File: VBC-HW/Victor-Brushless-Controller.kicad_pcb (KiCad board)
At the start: 2 copper layers, 44 x 44 mm, 85 parts, among them J1 i2c QWIIC, P1 V+, P2 GND, Q1 TPH4R008NH, Q2 TPH4R008NH, Q3 TPH4R008NH, Q4 TPH4R008NH, Q5 TPH4R008NH, Q6 TPH4R008NH, SW1 BOOT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

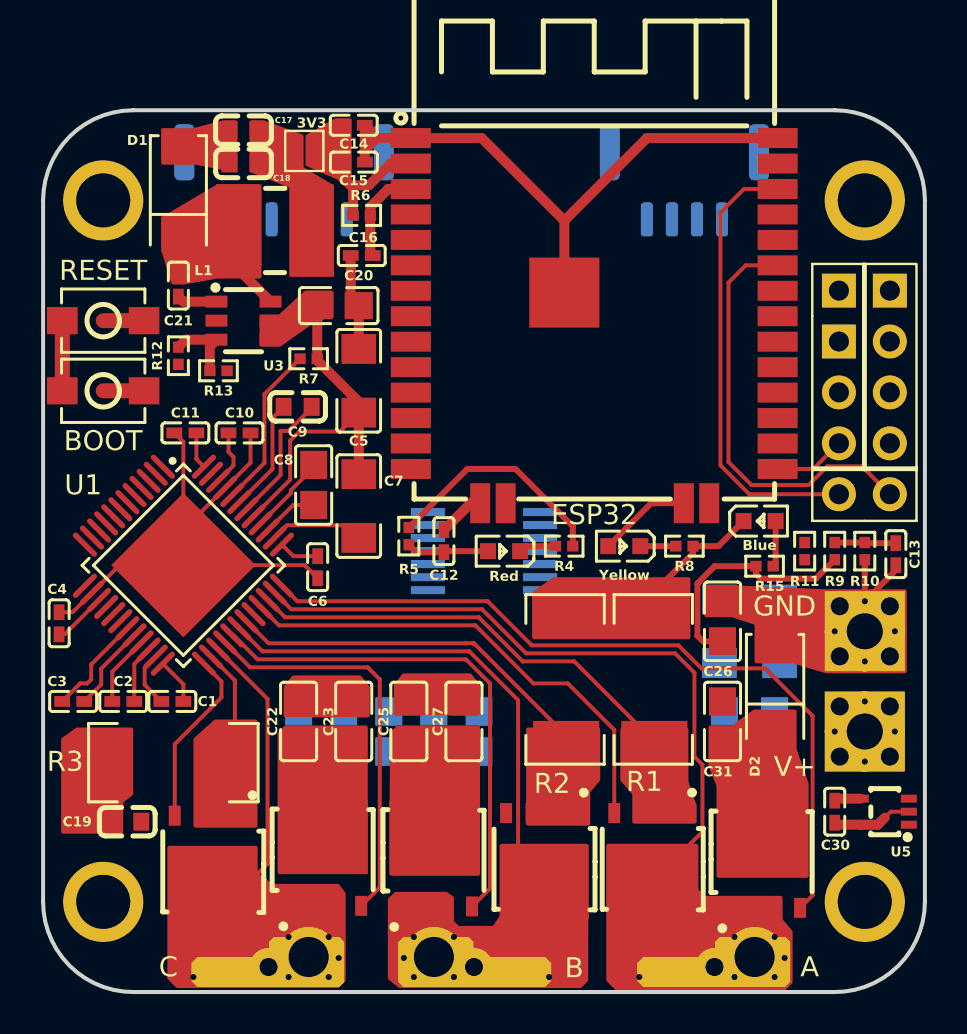
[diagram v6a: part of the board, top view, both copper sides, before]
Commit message: Finished vias and Inner layer 1
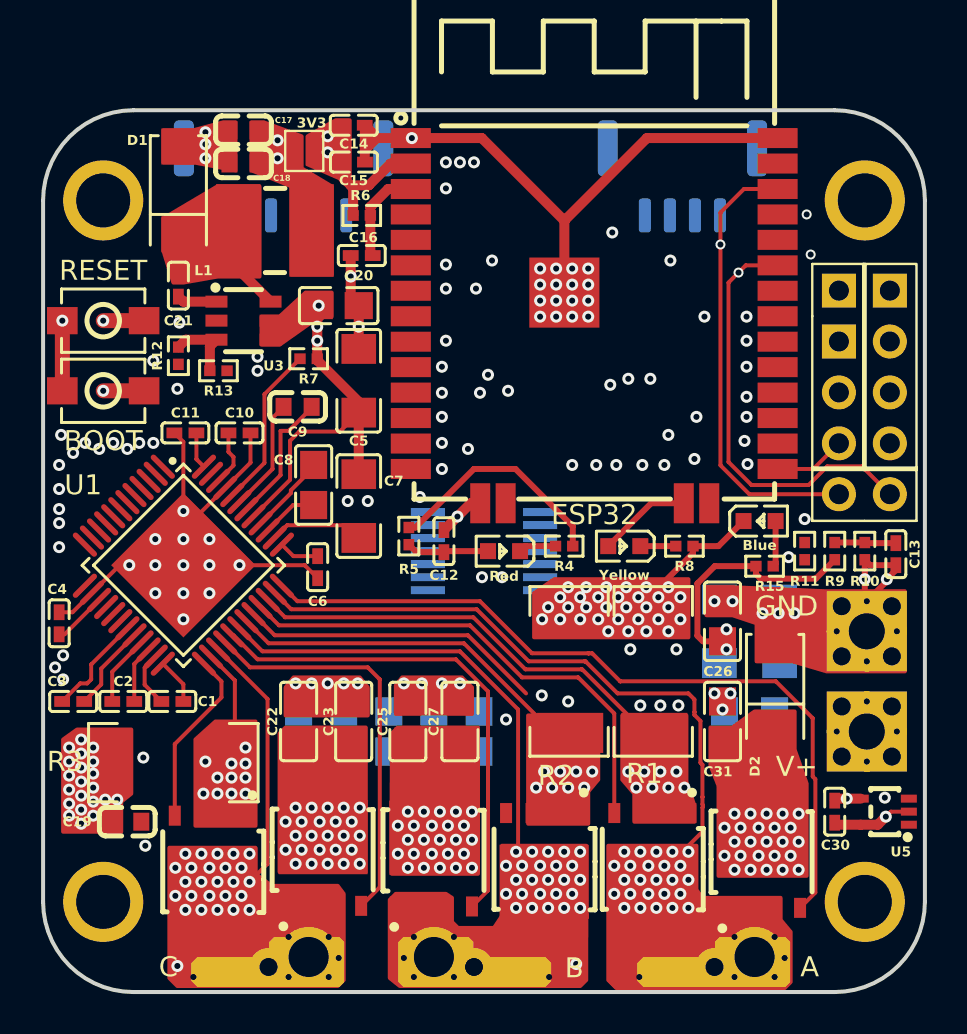
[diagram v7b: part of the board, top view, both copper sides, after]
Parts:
- J1: value i2c QWIIC -> i2c/UART
- U6: value External SPI -> SPI
- moved R2 0.45 mm to (183.8, 100.0)
- moved R1 0.40 mm to (188.0, 100.0)
- moved J1 0.22 mm to (189.4, 75.3)
- moved U6 0.20 mm to (169.5, 75.3)
- moved C27 0.20 mm to (178.3, 102.5)
- moved P1 0.10 mm to (198.6, 103.0)
- moved P2 0.10 mm to (198.6, 98.0)
- moved C25 0.05 mm to (175.7, 102.5)
- turned C36 to 90 degrees
- turned C37 to 90 degrees
- turned C38 to 90 degrees
- turned C39 to 90 degrees
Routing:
- net 3V3: track 0.00 -> 25.8 mm, vias 0 -> 4
- net /GLB: track 0.00 -> 15.2 mm
- net (no net): track 0.00 -> 12.2 mm, vias 0 -> 77
- net 3V3A: track 13.8 -> 25.0 mm, vias 0 -> 4
- net GND: track 94.8 -> 96.5 mm, vias 0 -> 110
- net /SLB: track 23.1 -> 22.0 mm, vias 0 -> 8
- net /PA: track 34.2 -> 33.5 mm, vias 0 -> 25
- net /PB: track 25.0 -> 24.7 mm, vias 0 -> 26
- net VCC: track 29.9 -> 29.8 mm, vias 0 -> 80
- net /SLA: vias 0 -> 8
- net IO21: vias 0 -> 1
- net RESET EN: vias 0 -> 1
- net IO22: vias 0 -> 1
- net BOOT IO0: vias 0 -> 1
- net /SLC: vias 0 -> 11
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- added copper zone on In1.Cu, net GND
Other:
- copper layers 2 -> 4

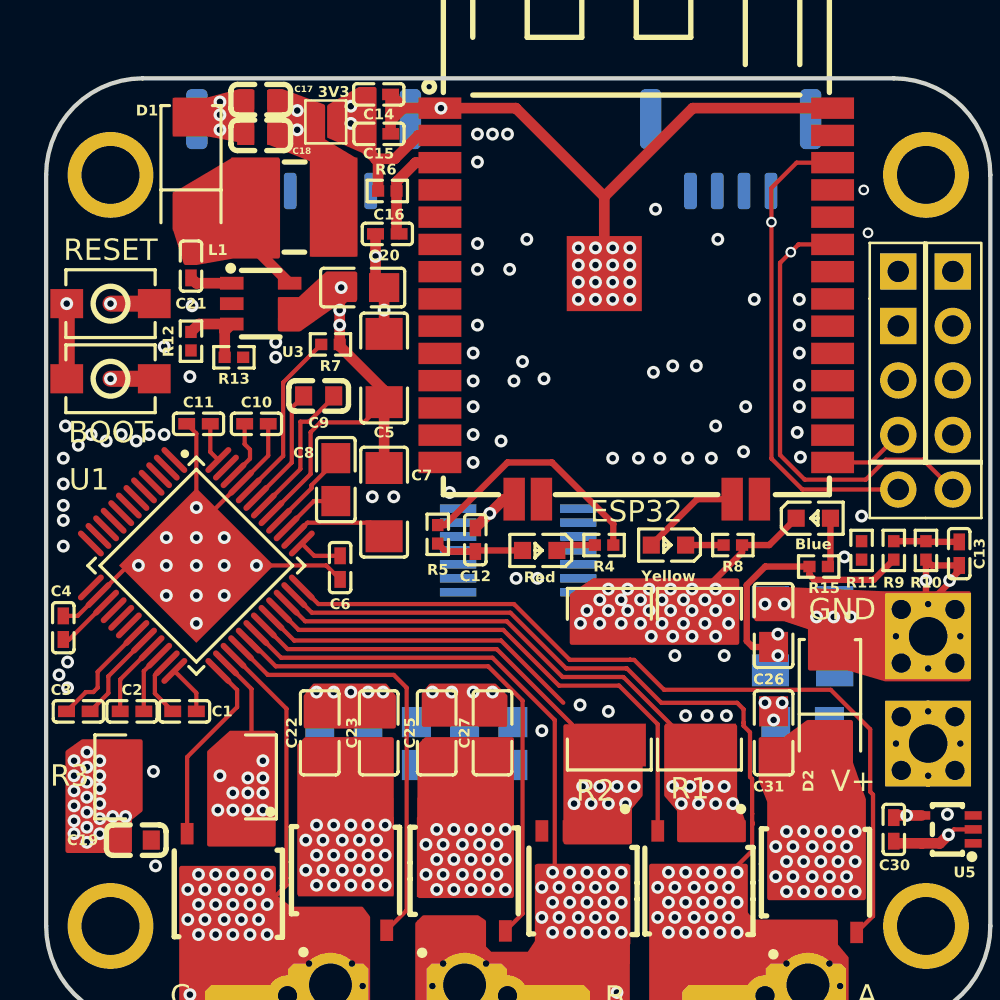
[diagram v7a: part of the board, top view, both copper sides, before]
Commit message: Started finishing vias conencting in top later
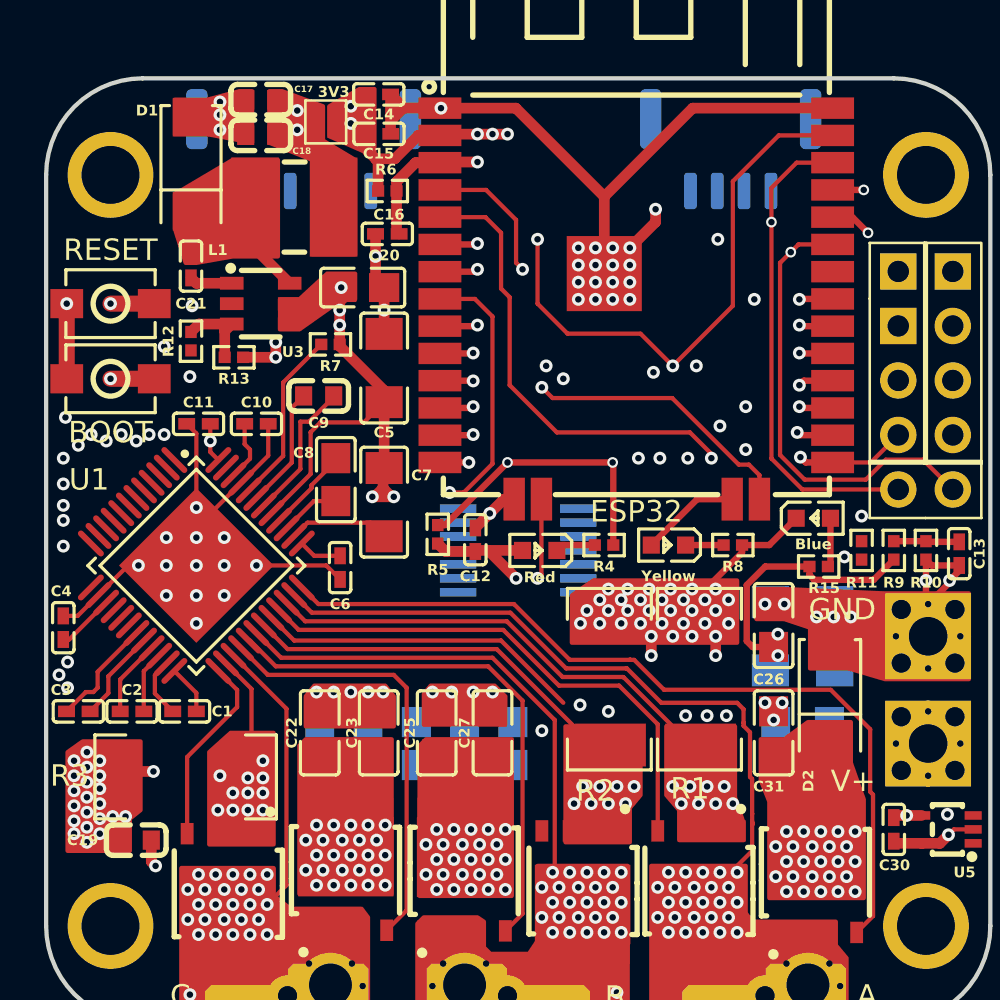
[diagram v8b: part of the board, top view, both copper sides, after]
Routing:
- net SDI MOSI23: track 0.00 -> 25.8 mm, vias 0 -> 2
- net Vtemp IO39: track 0.00 -> 21.3 mm, vias 0 -> 1
- net EN IO2: track 0.00 -> 13.0 mm, vias 0 -> 1
- net A IO32: track 0.00 -> 12.2 mm, vias 0 -> 1
- net GND: track 96.5 -> 104.4 mm, vias 110 -> 116
- net SO3 IO36: track 0.00 -> 6.55 mm, vias 0 -> 1
- net 3V3A: track 25.0 -> 30.0 mm, vias 4 -> 9
- net VCC: track 29.8 -> 34.4 mm, vias 80 -> 83
- net Z IO15: track 0.00 -> 3.76 mm, vias 0 -> 1
- net nFault IO4: track 11.6 -> 14.9 mm, vias 0 -> 3
- net RX0: track 0.00 -> 1.95 mm, vias 0 -> 1
- net SO2 IO35: track 0.00 -> 1.80 mm, vias 0 -> 1
- net Vbus IO33: track 3.06 -> 4.83 mm, vias 0 -> 1
- net SO1 IO34: track 0.00 -> 1.77 mm, vias 0 -> 1
- net RESET EN: track 6.91 -> 8.67 mm, vias 1 -> 2
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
